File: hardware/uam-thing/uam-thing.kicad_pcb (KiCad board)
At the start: 2 copper layers, 29 parts, among them J1 ESP_Left, J10 SFM_A, J11 SFM_C, J12 SFM_D, J2 ESP_Right, J3 PCA_Left, J4 PCA_Right, J5 MPX_A, J6 MPX_B, J7 MPX_C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

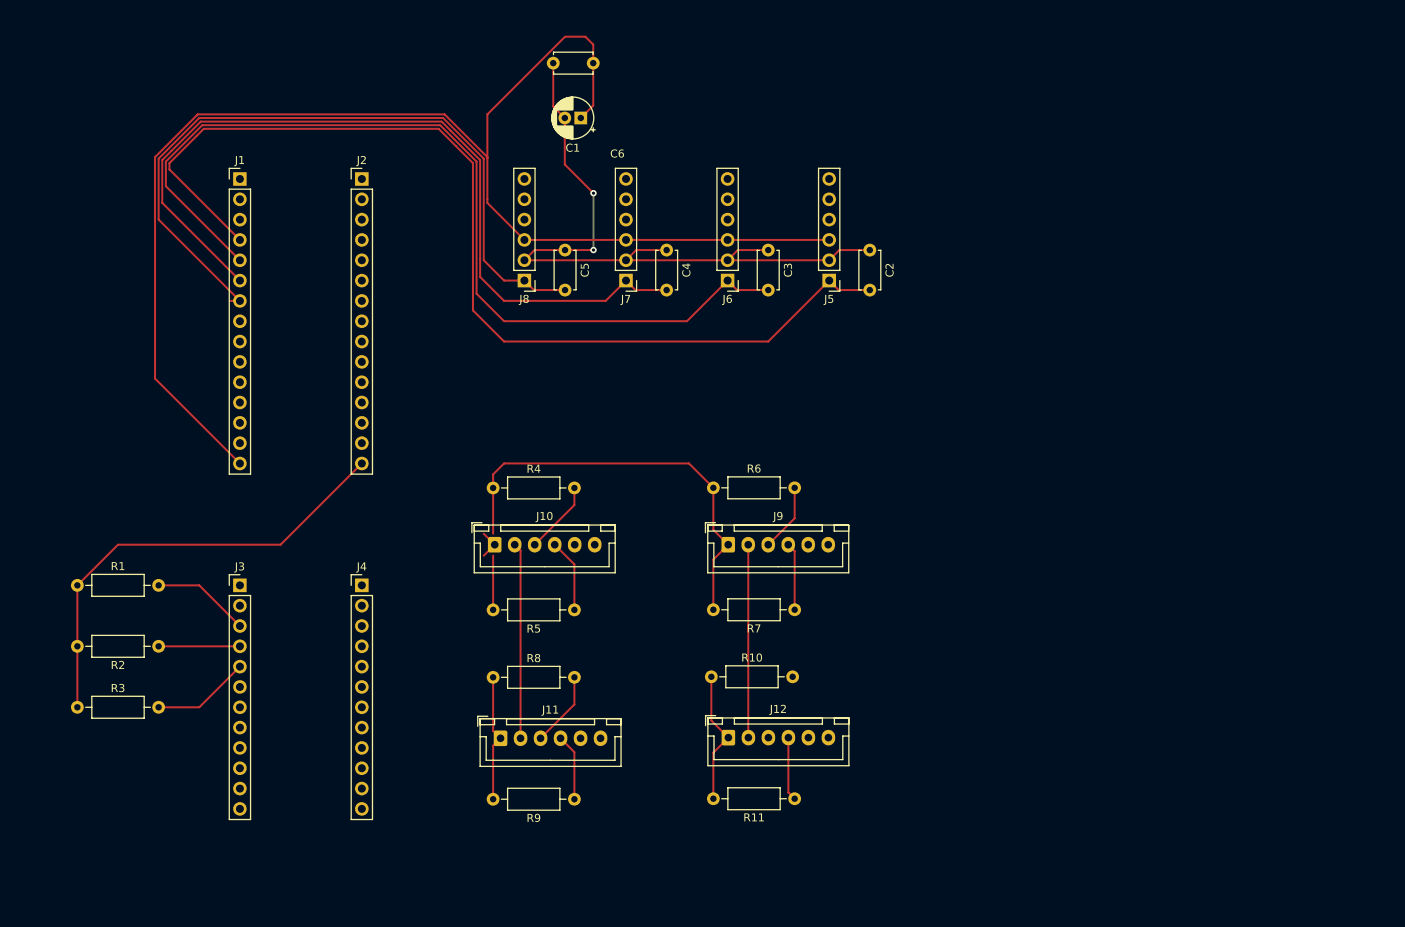
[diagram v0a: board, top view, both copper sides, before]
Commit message: Voltage dividers for MPX sensors
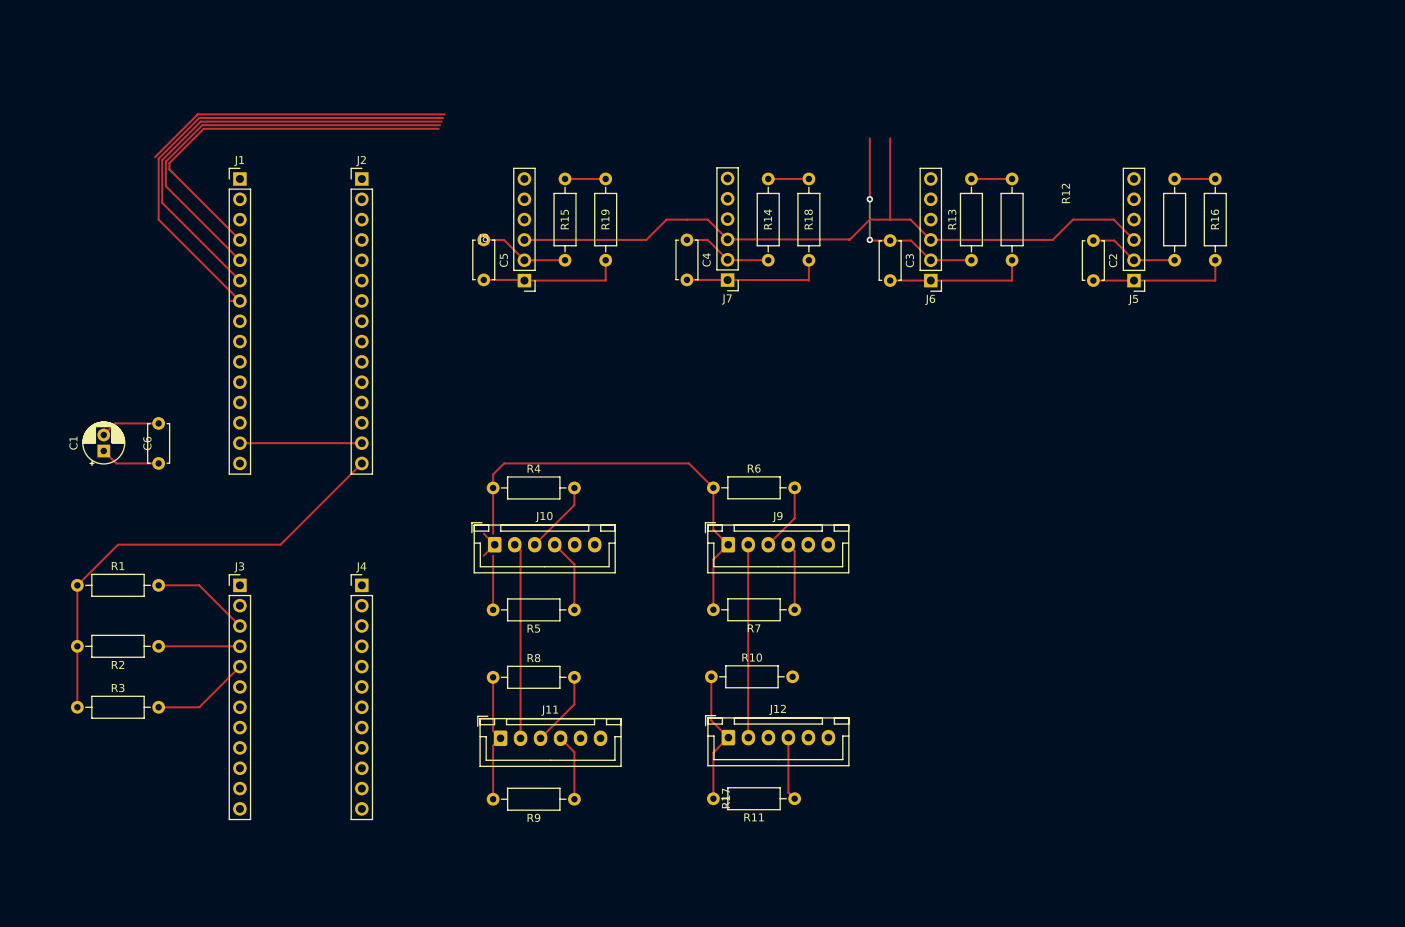
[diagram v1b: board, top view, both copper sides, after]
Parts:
- added R12: 100k, Resistor_THT:R_Axial_DIN0207_L6.3mm_D2.5mm_P10.16mm_Horizontal, F.Cu at (203.2, 91.4)
- added R13: 100k, Resistor_THT:R_Axial_DIN0207_L6.3mm_D2.5mm_P10.16mm_Horizontal, F.Cu at (177.8, 91.4)
- added R14: 100k, Resistor_THT:R_Axial_DIN0207_L6.3mm_D2.5mm_P10.16mm_Horizontal, F.Cu at (152.4, 91.4)
- added R15: 100k, Resistor_THT:R_Axial_DIN0207_L6.3mm_D2.5mm_P10.16mm_Horizontal, F.Cu at (127.0, 91.4)
- added R16: 100k, Resistor_THT:R_Axial_DIN0207_L6.3mm_D2.5mm_P10.16mm_Horizontal, F.Cu at (208.3, 81.3)
- added R17: 100k, Resistor_THT:R_Axial_DIN0207_L6.3mm_D2.5mm_P10.16mm_Horizontal, F.Cu at (182.9, 81.3)
- added R18: 100k, Resistor_THT:R_Axial_DIN0207_L6.3mm_D2.5mm_P10.16mm_Horizontal, F.Cu at (157.5, 81.3)
- added R19: 100k, Resistor_THT:R_Axial_DIN0207_L6.3mm_D2.5mm_P10.16mm_Horizontal, F.Cu at (132.1, 81.3)
- moved C6 73.9 mm to (76.2, 116.8), turned to 90 degrees
- moved C1 72.7 mm to (69.3, 115.3), turned to 90 degrees
- moved J5 38.1 mm to (198.1, 94.0)
- moved C2 28.0 mm to (193.0, 89.0)
- moved J6 25.4 mm to (172.7, 94.0)
- moved C3 15.3 mm to (167.6, 89.0)
- moved J7 12.7 mm to (147.3, 93.9)
- moved C5 10.2 mm to (116.8, 88.9)
- moved C4 2.84 mm to (142.2, 88.9)
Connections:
- C2 pad 2: /ADC1_CH6 -> Net-(C2-Pad2)
- C3 pad 2: /ADC1_CH7 -> Net-(C3-Pad2)
- C4 pad 2: /ADC1_CH4 -> Net-(C4-Pad2)
- C5 pad 2: /ADC1_CH5 -> Net-(C5-Pad2)
- J1 pad 14: unconnected-(J1-Pad14) -> GND
- J5 pad 1: /ADC1_CH6 -> Net-(C2-Pad2)
- J6 pad 1: /ADC1_CH7 -> Net-(C3-Pad2)
- J7 pad 1: /ADC1_CH4 -> Net-(C4-Pad2)
- J8 pad 1: /ADC1_CH5 -> Net-(C5-Pad2)
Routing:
- net /ADC1_CH6: track 128.0 -> 53.8 mm
- net /ADC1_CH7: track 115.8 -> 57.4 mm
- net /ADC1_CH4: track 103.5 -> 61.1 mm
- net +5V: track 269.1 -> 235.7 mm
- net /ADC1_CH5: track 92.5 -> 66.0 mm
- net Net-(C5-Pad2): track 0.00 -> 17.8 mm
- net Net-(C4-Pad2): track 0.00 -> 17.8 mm
- net Net-(C3-Pad2): track 0.00 -> 17.8 mm
- net Net-(C2-Pad2): track 0.00 -> 17.8 mm
- net GND: track 138.1 -> 131.4 mm

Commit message: Reworked PCB for 4 pin JST, replaced connectors again
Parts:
- J10, J11, J12, J9: footprint Connector_JST:JST_XH_B6B-XH-A_1x06_P2.50mm_Vertical -> Connector_JST:JST_XH_B4B-XH-A_1x04_P2.50mm_Vertical
- moved C5 107.0 mm to (223.5, 96.5), turned to 0 degrees
- moved J8 106.7 mm to (228.6, 91.4), turned to -90 degrees
- moved R15 99.2 mm to (226.1, 86.4), turned to 180 degrees
- moved R16 83.8 mm to (124.5, 81.3), turned to 0 degrees
- moved R19 83.8 mm to (215.9, 81.3), turned to 0 degrees
- moved R12 68.8 mm to (134.6, 86.4), turned to 180 degrees
- moved C2 61.3 mm to (132.2, 96.5), turned to 0 degrees
- moved J5 61.0 mm to (137.2, 91.4), turned to -90 degrees
- moved C4 51.4 mm to (193.1, 96.5), turned to 0 degrees
- moved J7 50.9 mm to (198.1, 91.4), turned to -90 degrees
- moved R14 43.5 mm to (195.6, 86.4), turned to 180 degrees
- moved R18 28.0 mm to (185.5, 81.3), turned to 0 degrees
- moved R17 27.9 mm to (154.9, 81.3), turned to 0 degrees
- moved R4 20.8 mm to (124.4, 139.7)
- moved R6 19.9 mm to (147.3, 139.7)
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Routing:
- net GND: track 131.4 -> 267.2 mm, vias 2 -> 0
- net /SFM_A_SCL: track 9.16 -> 139.7 mm
- net +5V: track 235.7 -> 361.1 mm, vias 0 -> 10
- net /ADC1_CH5: track 66.0 -> 173.3 mm
- net /SFM_A_SDL: track 9.15 -> 114.4 mm
- net /ADC1_CH4: track 61.1 -> 138.0 mm
- net /SFM_C_SCL: track 8.34 -> 76.2 mm
- net /SFM_C_SDL: track 9.37 -> 58.4 mm
- net /ADC1_CH7: track 57.4 -> 105.9 mm
- net /ADC1_CH6: track 53.8 -> 72.6 mm
- net /SFM_D_SDL: track 0.00 -> 12.7 mm
- net /SFM_B_SDL: track 8.48 -> 12.7 mm
- net /SFM_D_SCL: track 7.96 -> 10.2 mm
- net /SFM_B_SCL: track 8.46 -> 10.2 mm

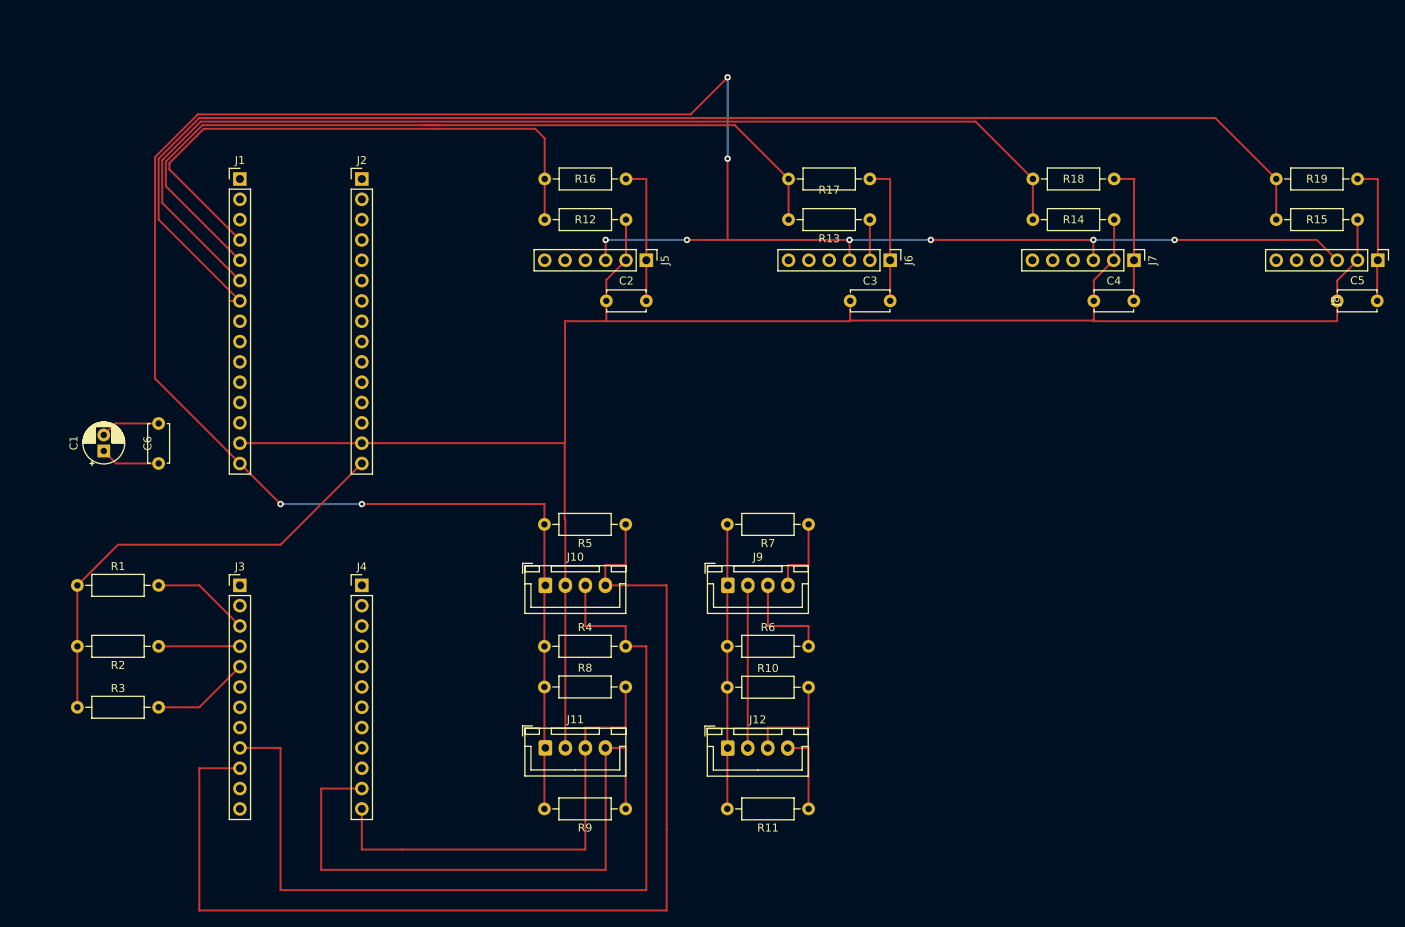
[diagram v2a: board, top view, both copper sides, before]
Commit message: Space saving PCB, now fits 100x100
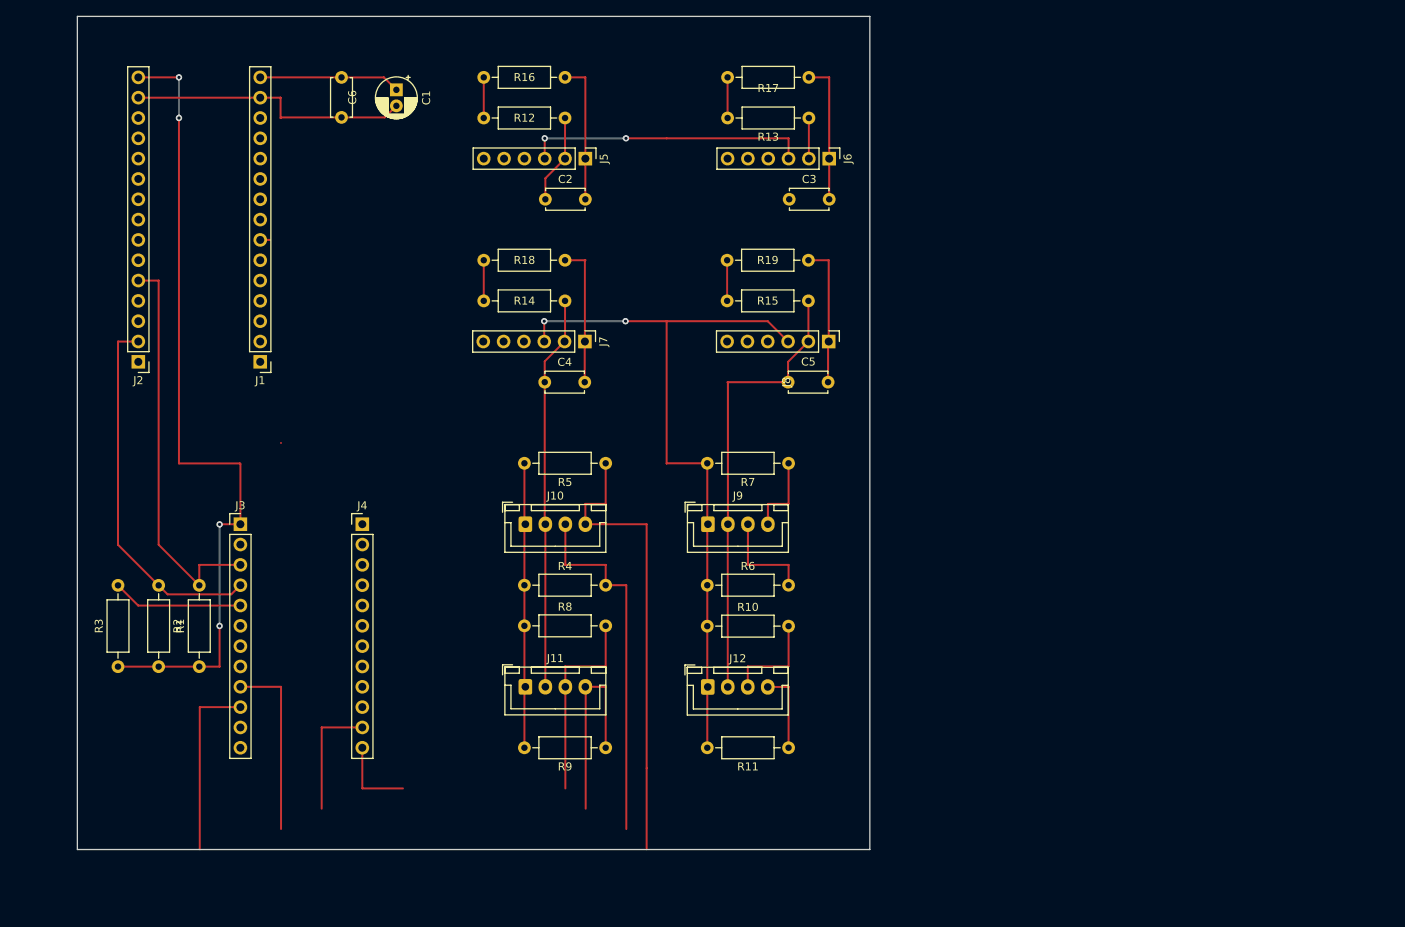
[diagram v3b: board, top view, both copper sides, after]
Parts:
- moved C5 69.4 mm to (154.9, 106.7)
- moved J7 69.4 mm to (129.5, 101.6)
- moved R15 69.4 mm to (157.4, 96.5)
- moved R19 69.4 mm to (147.3, 91.4)
- moved C4 69.4 mm to (124.5, 106.7)
- moved J8 69.4 mm to (160.0, 101.6)
- moved R14 69.4 mm to (127.0, 96.5)
- moved R18 69.4 mm to (116.8, 91.4)
- moved C1 58.1 mm to (105.9, 70.1), turned to -90 degrees
- moved C6 53.4 mm to (99.1, 68.6), turned to -90 degrees
- moved J2 36.1 mm to (73.7, 104.1), turned to 180 degrees
- moved J1 23.0 mm to (88.9, 104.1), turned to 180 degrees
- moved R1 18.3 mm to (81.3, 142.2), turned to 90 degrees
- moved J5 14.8 mm to (129.5, 78.7)
- moved R12 14.8 mm to (127.0, 73.7)
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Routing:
- net +5V: track 361.1 -> 182.2 mm, vias 10 -> 4
- net /ADC1_CH5: track 173.3 -> 6.35 mm
- net /ADC1_CH4: track 138.0 -> 5.08 mm
- net GND: track 267.2 -> 158.0 mm
- net /ADC1_CH7: track 105.9 -> 5.08 mm
- net /ADC1_CH6: track 72.6 -> 5.08 mm
- net /SFM_A_SCL: track 139.7 -> 81.3 mm
- net /SFM_A_SDL: track 114.4 -> 68.6 mm
- net +3.3V: track 57.1 -> 101.8 mm, vias 0 -> 4
- net /SDA_ESP: track 12.3 -> 50.5 mm
- net /SCL_ESP: track 10.2 -> 46.3 mm
- net /SFM_C_SCL: track 76.2 -> 40.6 mm
- net /SFM_C_SDL: track 58.4 -> 35.6 mm
- net Net-(J3-Pad5): track 12.3 -> 16.3 mm
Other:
- board outline added: 99.1 x 104.1 mm

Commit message: Updated header footprints
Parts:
- moved J5 38.1 mm to (160.0, 101.6)
- moved C2 38.1 mm to (155.0, 106.7)
- moved R12 38.1 mm to (157.5, 96.5)
- moved R16 38.1 mm to (147.3, 91.4)
- moved J8 38.1 mm to (129.5, 78.7)
- moved C5 38.1 mm to (124.5, 83.8)
- moved R15 38.1 mm to (127.0, 73.7)
- moved R19 38.1 mm to (116.8, 68.6)
- moved J2 10.2 mm to (63.5, 104.1)
- moved J4 2.48 mm to (104.1, 124.5)
- moved C1 1.78 mm to (104.1, 70.1)
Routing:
- net /ADC1_CH7: track 5.08 -> 83.8 mm, vias 0 -> 2
- net /SFM_A_SCL: track 81.3 -> 10.2 mm
- net /ADC1_CH6: track 5.08 -> 73.7 mm, vias 0 -> 2
- net /SFM_A_SDL: track 68.6 -> 12.7 mm
- net /ADC1_CH5: track 6.35 -> 48.3 mm
- net /SFM_C_SCL: track 40.6 -> 10.2 mm
- net /ADC1_CH4: track 5.08 -> 33.0 mm
- net /SFM_C_SDL: track 35.6 -> 12.7 mm
- net +5V: track 182.2 -> 198.2 mm, vias 4 -> 2
- net GND: track 158.0 -> 168.2 mm, vias 0 -> 2
- net +3.3V: track 101.8 -> 109.9 mm, vias 4 -> 2
- net /SCL_ESP: track 46.3 -> 54.3 mm
- net /SDA_ESP: track 50.5 -> 57.9 mm
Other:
- board size 99.1 x 104.1 mm -> 106.7 x 94 mm

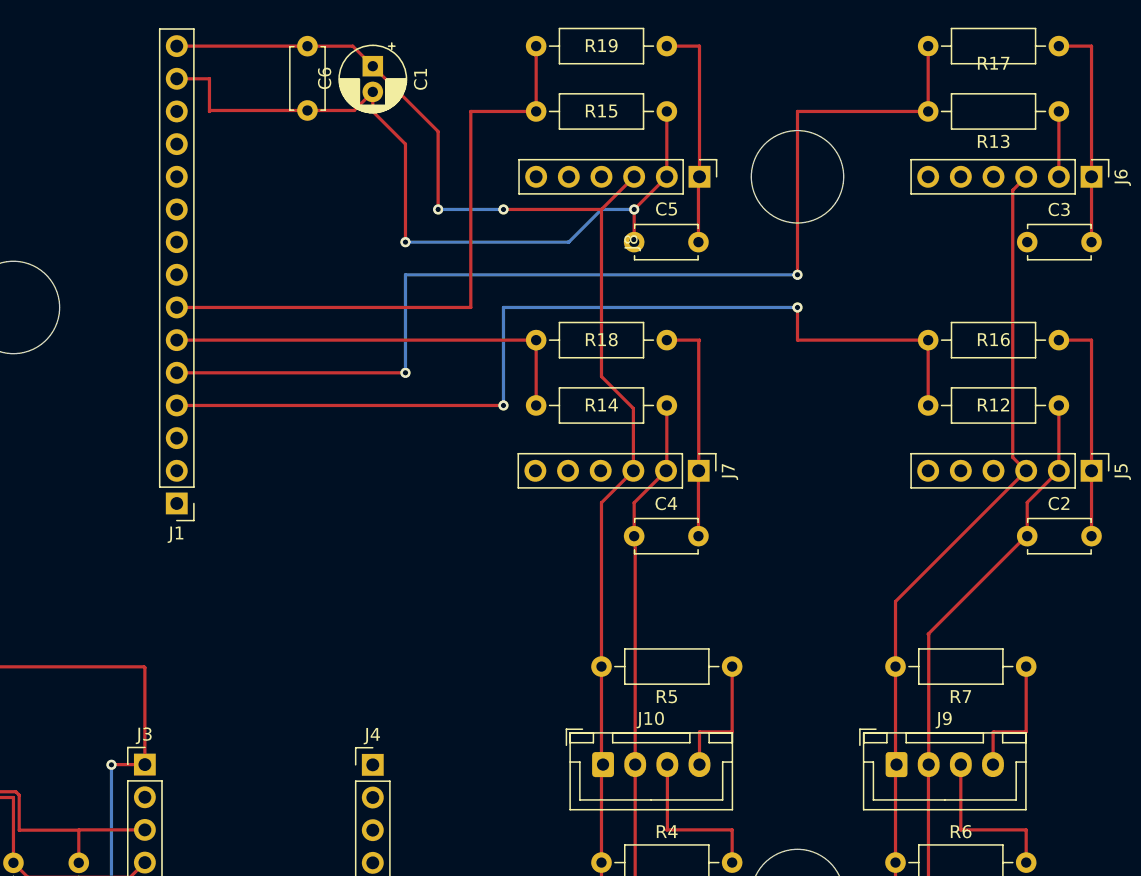
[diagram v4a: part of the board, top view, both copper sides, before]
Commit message: Reorganized 5V and GND lines
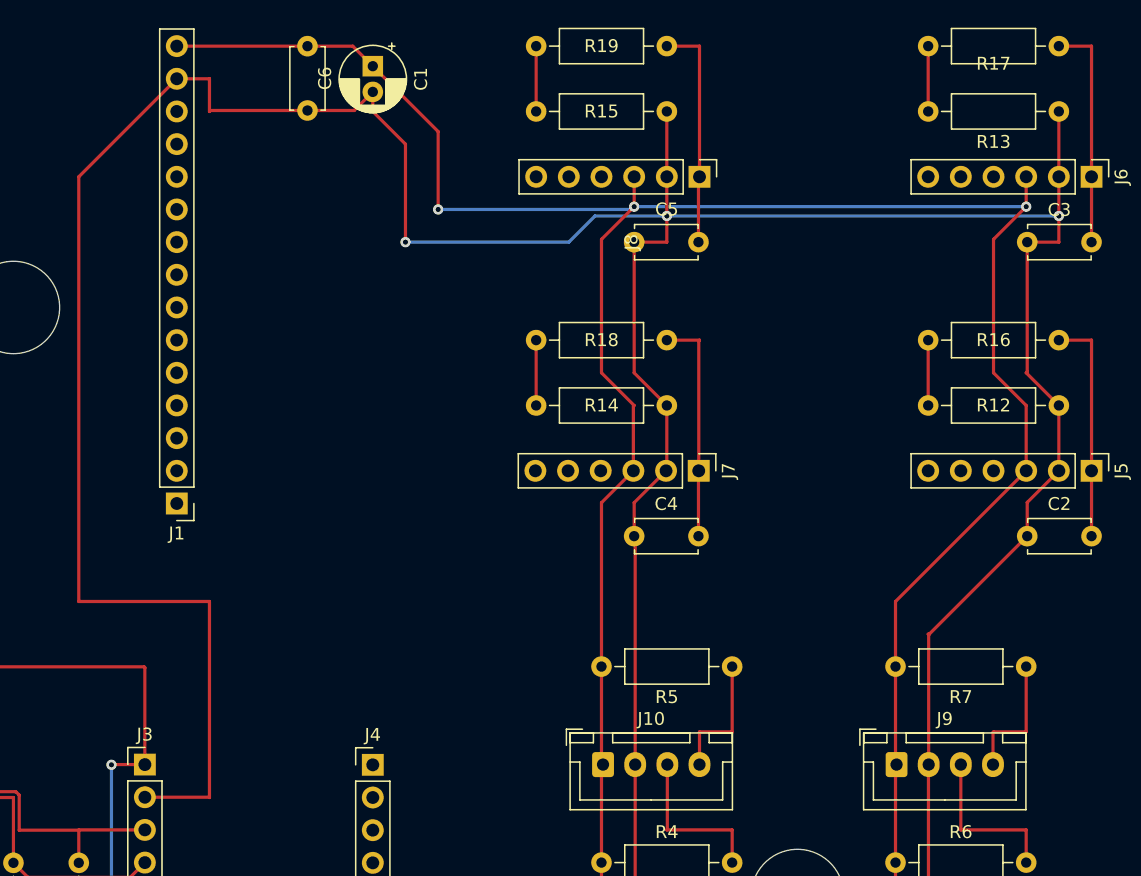
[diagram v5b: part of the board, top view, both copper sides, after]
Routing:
- net GND: track 168.2 -> 311.9 mm, vias 2 -> 3
- net /ADC1_CH7: track 83.8 -> 5.08 mm, vias 2 -> 0
- net /ADC1_CH6: track 73.7 -> 5.08 mm, vias 2 -> 0
- net /ADC1_CH5: track 48.3 -> 5.08 mm
- net +5V: track 198.2 -> 232.6 mm, vias 2 -> 3
- net /ADC1_CH4: track 33.0 -> 5.08 mm
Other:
- outline, holes or cut-outs redrawn
